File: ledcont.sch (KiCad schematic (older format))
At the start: 27 parts, among them J1 Screw_Terminal_01x02, J2 Screw_Terminal_01x02, U1 PAM2804, U2 MCP6002-xSN

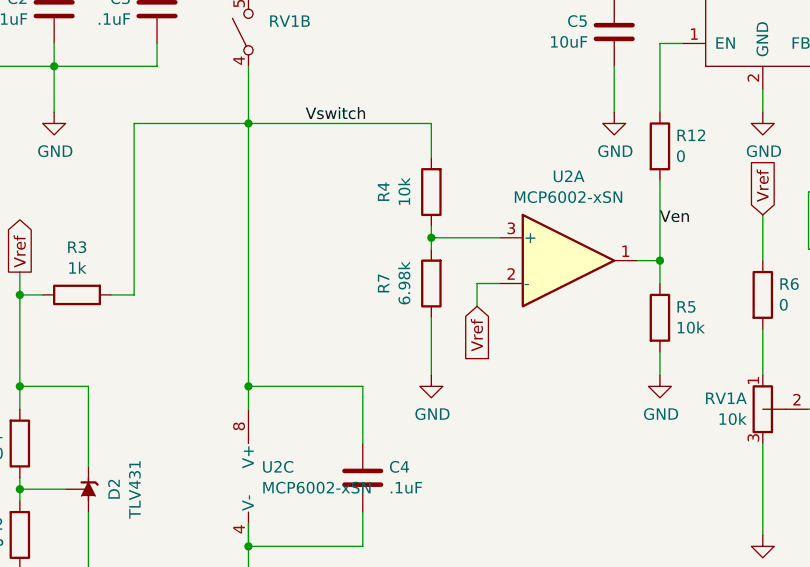
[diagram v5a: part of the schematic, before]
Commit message: Compensate for D1's forward drop.
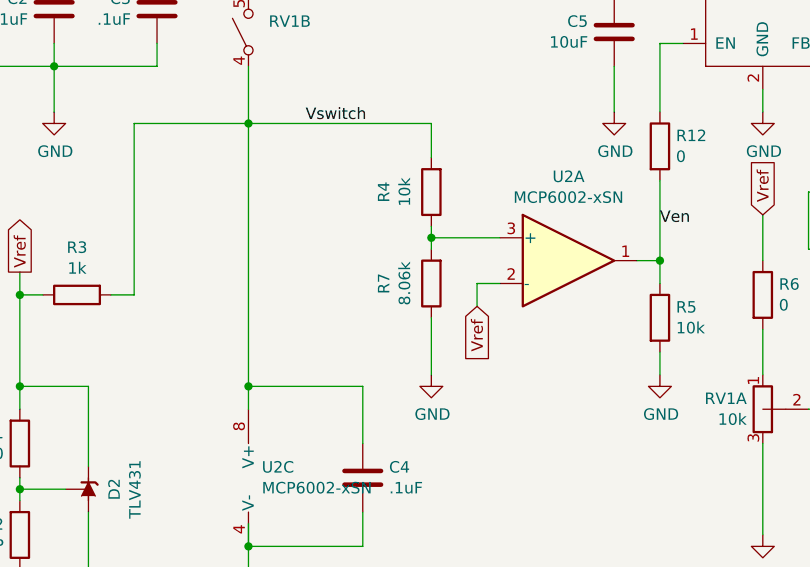
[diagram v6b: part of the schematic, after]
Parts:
- R7: value 6.98k -> 8.06k; Part RC0603FR-076K98L -> RC0603FR-078K06L
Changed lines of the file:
@@
 P 5800 3450
 F 0 "R7" V 6007 3450 50  0000 C CNN
-F 1 "6.98k" V 5916 3450 50  0000 C CNN
+F 1 "8.06k" V 5916 3450 50  0000 C CNN
 F 2 "Resistor_SMD:R_0603_1608Metric_Pad1.05x0.95mm_HandSolder" V 5730 3450 50  0001 C CNN
 F 3 "~" H 5800 3450 50  0001 C CNN
-F 4 "RC0603FR-076K98L" H -1600 400 50  0001 C CNN "Part"
+F 4 "RC0603FR-078K06L" H -1600 400 50  0001 C CNN "Part"
 F 5 "1%" H -1600 400 50  0001 C CNN "Tolerance"
 	1    5800 3450

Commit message: Add part vendors.
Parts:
- C1, C2, C3, C4, C5, C6: Vendor (none) -> Samsung
- D1: Vendor (none) -> On Semiconductor
- D2, U1: Vendor (none) -> Diodes Inc.
- J1, J2: Vendor (none) -> Phoenix Contact
- L1: Vendor (none) -> Murata
- R1, R10, R11, R12, R3, R4, R5, R6, R7, R8, R9: Vendor (none) -> Yageo
- R2: Tolerance 1% -> (none)
- RV1: Vendor (none) -> TT Electronics
- RV2: Vendor (none) -> Bourns Inc.
- U2: Vendor (none) -> Microchip Technology
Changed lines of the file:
@@
 F 4 "1%" H 700 0   50  0001 C CNN "Tolerance"
 F 5 "RC1206FR-071KL" H 700 0   50  0001 C CNN "Part"
+F 6 "Yageo" H 0   0   50  0001 C CNN "Vendor"
 	1    8600 3050
 	0    -1   -1   0
@@
 F 4 "PT1206FR-070R2L" H 700 0   50  0001 C CNN "Part"
 F 5 "1%" H 700 0   50  0001 C CNN "Tolerance"
+F 6 "Yageo" H 0   0   50  0001 C CNN "Vendor"
 	1    9400 3300
 	1    0    0    -1
@@
 F 3 "~" H 8850 2350 50  0001 C CNN
 F 4 "CL31B106KOHNFNE" H 700 0   50  0001 C CNN "Part"
+F 5 "Samsung" H 0   0   50  0001 C CNN "Vendor"
 	1    8850 2350
 	1    0    0    -1
@@
 F 3 "~" H 8550 2100 50  0001 C CNN
 F 4 "LQH43PN4R7M26L" H 700 0   50  0001 C CNN "Part"
+F 5 "Murata" H 0   0   50  0001 C CNN "Vendor"
 	1    8550 2100
 	0    -1   -1   0
@@
 F 3 "~" H 6600 2350 50  0001 C CNN
 F 4 "CL31B106KOHNFNE" H 700 0   50  0001 C CNN "Part"
+F 5 "Samsung" H 0   0   50  0001 C CNN "Vendor"
 	1    6600 2350
 	1    0    0    -1
@@
 F 3 "~" H 9600 2100 50  0001 C CNN
 F 4 "1984617" H 700 0   50  0001 C CNN "Part"
+F 5 "Phoenix Contact" H 0   0   50  0001 C CNN "Vendor"
 	1    9600 2100
 	1    0    0    -1
@@
 F 3 "~" H 2750 2100 50  0001 C CNN
 F 4 "1984617" H 0   0   50  0001 C CNN "Part"
+F 5 "Phoenix Contact" H 0   0   50  0001 C CNN "Vendor"
 	1    2750 2100
 	-1   0    0    -1
@@
 F 3 "~" H 7250 4000 50  0001 C CNN
 F 4 "P091S-FC20BR10K" H 500 -200 50  0001 C CNN "Part"
+F 5 "TT Electronics" H 0   0   50  0001 C CNN "Vendor"
 	1    7250 4000
 	1    0    0    1
@@
 F 3 "~" H 4950 2350 50  0001 C CNN
 F 4 "P091S-FC20BR10K" H 0   0   50  0001 C CNN "Part"
+F 5 "TT Electronics" H 0   0   50  0001 C CNN "Vendor"
 	2    4950 2350
 	1    0    0    -1
@@
 F 4 "1%" H -200 0   50  0001 C CNN "Tolerance"
 F 5 "RC0603FR-071KL" V 4250 3500 50  0001 C CNN "Part"
+F 6 "Yageo" H 0   0   50  0001 C CNN "Vendor"
 	1    4250 3500
 	0    -1   1    0
@@
 F 4 "1%" H 4000 4150 50  0001 C CNN "Tolerance"
 F 5 "RC0603FR-070RL" H -200 0   50  0001 C CNN "Part"
+F 6 "Yageo" H 4000 4150 50  0001 C CNN "Vendor"
 	1    4000 4150
 	1    0    0    1
@@
 F 2 "Resistor_SMD:R_0603_1608Metric_Pad1.05x0.95mm_HandSolder" V 3930 4550 50  0001 C CNN
 F 3 "~" H 4000 4550 50  0001 C CNN
-F 4 "1%" H -200 0   50  0001 C CNN "Tolerance"
+F 4 "" H -200 0   50  0001 C CNN "Tolerance"
 F 5 "" H -200 0   50  0001 C CNN "Part"
 	1    4000 4550
@@
 F 3 "~" H 7250 3500 50  0001 C CNN
 F 4 "RC0603FR-070RL" H 500 -300 50  0001 C CNN "Part"
+F 5 "Yageo" H 0   0   50  0001 C CNN "Vendor"
 	1    7250 3500
 	1    0    0    -1
@@
 F 3 "~" H 3400 2100 50  0001 C CNN
 F 4 "NRVTS245ESFT1G" H 0   0   50  0001 C CNN "Part"
+F 5 "On Semiconductor" H 0   0   50  0001 C CNN "Vendor"
 	1    3400 2100
 	-1   0    0    1
@@
 F 3 "~" H 3750 2250 50  0001 C CNN
 F 4 "CL31B106KOHNFNE" H 0   0   50  0001 C CNN "Part"
+F 5 "Samsung" H 0   0   50  0001 C CNN "Vendor"
 	1    3750 2250
 	1    0    0    -1
@@
 F 3 "~" H 4150 2250 50  0001 C CNN
 F 4 "CL31B105MAHNNNE" H 0   0   50  0001 C CNN "Part"
+F 5 "Samsung" H 0   0   50  0001 C CNN "Vendor"
 	1    4150 2250
 	1    0    0    -1
@@
 F 3 "~" H 4600 2250 50  0001 C CNN
 F 4 "CL31B104KBCNNNC" H 0   0   50  0001 C CNN "Part"
+F 5 "Samsung" H 0   0   50  0001 C CNN "Vendor"
 	1    4600 2250
 	1    0    0    -1
@@
 F 4 "1%" H 700 0   50  0001 C CNN "Tolerance"
 F 5 "RC0603FR-0710KL" H 700 0   50  0001 C CNN "Part"
+F 6 "Yageo" H 0   0   50  0001 C CNN "Vendor"
 	1    6800 3600
 	1    0    0    -1
@@
 F 3 "~" H 5500 4300 50  0001 C CNN
 F 4 "CL31B104KBCNNNC" H 550 350 50  0001 C CNN "Part"
+F 5 "Samsung" H 0   0   50  0001 C CNN "Vendor"
 	1    5500 4300
 	1    0    0    -1
@@
 F 3 "" H 7250 2250 50  0001 C CNN
 F 4 "PAM2804AAB010" H 700 0   50  0001 C CNN "Part"
+F 5 "Diodes Inc." H 0   0   50  0001 C CNN "Vendor"
 	1    7250 2250
 	1    0    0    -1
@@
 F 3 "http://ww1.microchip.com/downloads/en/DeviceDoc/21733j.pdf" H 6400 3350 50  0001 C CNN
 F 4 "MCP6002T-I/SN" H 0   0   50  0001 C CNN "Part"
+F 5 "Microchip Technology" H 0   0   50  0001 C CNN "Vendor"
 	1    6400 3350
 	1    0    0    -1
@@
 F 3 "http://ww1.microchip.com/downloads/en/DeviceDoc/21733j.pdf" H 8150 4100 50  0001 C CNN
 F 4 "MCP6002T-I/SN" H 0   0   50  0001 C CNN "Part"
+F 5 "Microchip Technology" H 0   0   50  0001 C CNN "Vendor"
 	2    8150 4100
 	1    0    0    -1
@@
 F 3 "http://ww1.microchip.com/downloads/en/DeviceDoc/21733j.pdf" H 5100 4300 50  0001 C CNN
 F 4 "MCP6002T-I/SN" H 0   0   50  0001 C CNN "Part"
+F 5 "Microchip Technology" H 0   0   50  0001 C CNN "Vendor"
 	3    5100 4300
 	1    0    0    -1
@@
 F 3 "http://www.ti.com/lit/ds/symlink/tl431.pdf" H 4300 4350 50  0001 C CIN
 F 4 "TLV431AFTA" H 4300 4350 50  0001 C CNN "Part"
+F 5 "Diodes Inc." H 0   0   50  0001 C CNN "Vendor"
 	1    4300 4350
 	0    -1   -1   0
@@
 F 4 "1%" H -2100 0   50  0001 C CNN "Tolerance"
 F 5 "RC0603FR-0710KL" H -2100 0   50  0001 C CNN "Part"
+F 6 "Yageo" H 0   0   50  0001 C CNN "Vendor"
 	1    5800 3050
 	-1   0    0    1
@@
 F 4 "RC0603FR-078K06L" H -1600 400 50  0001 C CNN "Part"
 F 5 "1%" H -1600 400 50  0001 C CNN "Tolerance"
+F 6 "Yageo" H 0   0   50  0001 C CNN "Vendor"
 	1    5800 3450
 	-1   0    0    1
@@
 F 3 "~" H 7700 3050 50  0001 C CNN
 F 4 "TC33X-2-502E" V 7700 3050 50  0001 C CNN "Part"
+F 5 "Bourns Inc." H 0   0   50  0001 C CNN "Vendor"
 	1    7700 3050
 	0    -1   1    0
@@
 F 4 "1%" H 200 0   50  0001 C CNN "Tolerance"
 F 5 "RC0603FR-0710KL" H 200 0   50  0001 C CNN "Part"
+F 6 "Yageo" H 0   0   50  0001 C CNN "Vendor"
 	1    8100 3050
 	0    -1   -1   0
@@
 F 3 "~" H 8550 3850 50  0001 C CNN
 F 4 "RC0603FR-070RL" H 1800 50  50  0001 C CNN "Part"
+F 5 "Yageo" H 0   0   50  0001 C CNN "Vendor"
 	1    8550 3850
 	1    0    0    -1
@@
 F 3 "~" H 6800 2850 50  0001 C CNN
 F 4 "RC0603FR-070RL" H 50  -950 50  0001 C CNN "Part"
+F 5 "Yageo" H 0   0   50  0001 C CNN "Vendor"
 	1    6800 2850
 	1    0    0    -1

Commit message: Fix vendors.
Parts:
- D1: Vendor On Semiconductor -> ON Semiconductor
- RV1: Vendor TT Electronics -> BI Electronics
- RV2: Vendor Bourns Inc. -> Bourns
- U2: Vendor Microchip Technology -> Microchip
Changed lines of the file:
@@
 F 3 "~" H 7250 4000 50  0001 C CNN
 F 4 "P091S-FC20BR10K" H 500 -200 50  0001 C CNN "Part"
-F 5 "TT Electronics" H 0   0   50  0001 C CNN "Vendor"
+F 5 "BI Electronics" H 0   0   50  0001 C CNN "Vendor"
 	1    7250 4000
 	1    0    0    1
@@
 F 3 "~" H 4950 2350 50  0001 C CNN
 F 4 "P091S-FC20BR10K" H 0   0   50  0001 C CNN "Part"
-F 5 "TT Electronics" H 0   0   50  0001 C CNN "Vendor"
+F 5 "BI Electronics" H 0   0   50  0001 C CNN "Vendor"
 	2    4950 2350
 	1    0    0    -1
@@
 F 3 "~" H 3400 2100 50  0001 C CNN
 F 4 "NRVTS245ESFT1G" H 0   0   50  0001 C CNN "Part"
-F 5 "On Semiconductor" H 0   0   50  0001 C CNN "Vendor"
+F 5 "ON Semiconductor" H 0   0   50  0001 C CNN "Vendor"
 	1    3400 2100
 	-1   0    0    1
@@
 F 3 "http://ww1.microchip.com/downloads/en/DeviceDoc/21733j.pdf" H 6400 3350 50  0001 C CNN
 F 4 "MCP6002T-I/SN" H 0   0   50  0001 C CNN "Part"
-F 5 "Microchip Technology" H 0   0   50  0001 C CNN "Vendor"
+F 5 "Microchip" H 0   0   50  0001 C CNN "Vendor"
 	1    6400 3350
 	1    0    0    -1
@@
 F 3 "http://ww1.microchip.com/downloads/en/DeviceDoc/21733j.pdf" H 8150 4100 50  0001 C CNN
 F 4 "MCP6002T-I/SN" H 0   0   50  0001 C CNN "Part"
-F 5 "Microchip Technology" H 0   0   50  0001 C CNN "Vendor"
+F 5 "Microchip" H 0   0   50  0001 C CNN "Vendor"
 	2    8150 4100
 	1    0    0    -1
@@
 F 3 "http://ww1.microchip.com/downloads/en/DeviceDoc/21733j.pdf" H 5100 4300 50  0001 C CNN
 F 4 "MCP6002T-I/SN" H 0   0   50  0001 C CNN "Part"
-F 5 "Microchip Technology" H 0   0   50  0001 C CNN "Vendor"
+F 5 "Microchip" H 0   0   50  0001 C CNN "Vendor"
 	3    5100 4300
 	1    0    0    -1
@@
 F 3 "~" H 7700 3050 50  0001 C CNN
 F 4 "TC33X-2-502E" V 7700 3050 50  0001 C CNN "Part"
-F 5 "Bourns Inc." H 0   0   50  0001 C CNN "Vendor"
+F 5 "Bourns" H 0   0   50  0001 C CNN "Vendor"
 	1    7700 3050
 	0    -1   1    0
